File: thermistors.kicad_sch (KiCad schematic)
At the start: 6 parts, among them J6 Conn_02x10_Counter_Clockwise, J7 Conn_02x10_Counter_Clockwise, J8 Conn_02x10_Counter_Clockwise

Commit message: schematic: MCU cleanup
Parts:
- J6, J7, J8: footprint (none) -> Connector_JST:JST_PUD_S20B-PUDSS-1_2x10_P2.00mm_Horizontal; Part Number (none) -> S20B-PUDSS-1
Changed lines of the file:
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@@
 			)
 		)
-		(property "Footprint" ""
+		(property "Footprint" "Connector_JST:JST_PUD_S20B-PUDSS-1_2x10_P2.00mm_Horizontal"
 			(at 139.7 69.85 0)
 			(effects
@@
 		)
 		(property "Description" "Generic connector, double row, 02x10, counter clockwise pin numbering scheme (similar to DIP package numbering), script generated (kicad-library-utils/schlib/autogen/connector/)"
+			(at 139.7 69.85 0)
+			(effects
+				(font
+					(size 1.27 1.27)
+				)
+				(hide yes)
+			)
+		)
+		(property "Part Number" "S20B-PUDSS-1"
 			(at 139.7 69.85 0)
 			(effects
@@
 			)
 		)
-		(property "Footprint" ""
+		(property "Footprint" "Connector_JST:JST_PUD_S20B-PUDSS-1_2x10_P2.00mm_Horizontal"
 			(at 139.7 95.25 0)
 			(effects
@@
 		)
 		(property "Description" "Generic connector, double row, 02x10, counter clockwise pin numbering scheme (similar to DIP package numbering), script generated (kicad-library-utils/schlib/autogen/connector/)"
+			(at 139.7 95.25 0)
+			(effects
+				(font
+					(size 1.27 1.27)
+				)
+				(hide yes)
+			)
+		)
+		(property "Part Number" "S20B-PUDSS-1"
 			(at 139.7 95.25 0)
 			(effects
@@
 			)
 		)
-		(property "Footprint" ""
+		(property "Footprint" "Connector_JST:JST_PUD_S20B-PUDSS-1_2x10_P2.00mm_Horizontal"
 			(at 139.7 120.65 0)
 			(effects
@@
 			(at 139.7 120.65 0)
 			(effects
+				(font
+					(size 1.27 1.27)
+				)
+				(hide yes)
+			)
+		)
+		(property "Part Number" "S20B-PUDSS-1"
+			(at 139.7 120.65 0)
+			(effects

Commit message: schematic: Cleanup
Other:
- company: (none) -> York Formula Student
- title: (none) -> Battery Management System
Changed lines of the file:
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@@
 	(generator_version "8.0")
 	(paper "A4")
+	(title_block
+		(title "Battery Management System")
+		(date "2025-02-08")
+		(rev "1")
+		(company "York Formula Student")
+	)
 	(wire
 		(pts

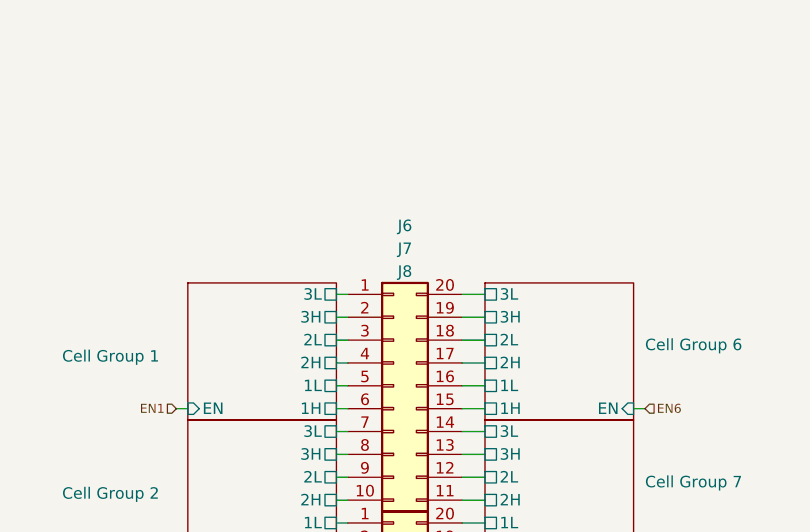
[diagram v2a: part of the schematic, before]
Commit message: schematic: Re-annotate designators
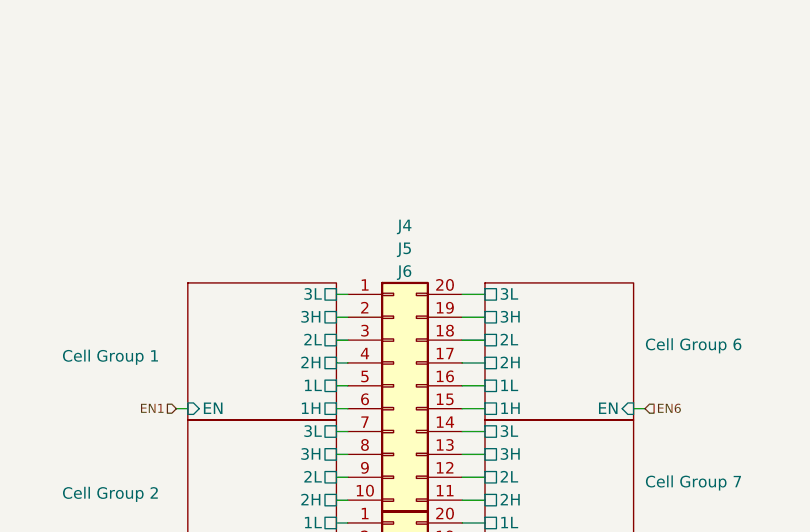
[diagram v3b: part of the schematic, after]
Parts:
- J4: renamed from J6; value Conn_02x10_Counter_Clockwise -> THERM_1; Role (none) -> Thermistor connector
- J5: renamed from J7; value Conn_02x10_Counter_Clockwise -> THERM_2; Role (none) -> Thermistor connector
- J6: renamed from J8; value Conn_02x10_Counter_Clockwise -> THERM_3; Role (none) -> Thermistor connector
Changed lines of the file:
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@@
 		(on_board yes)
 		(dnp no)
-		(property "Reference" "J6"
+		(property "Reference" "J4"
 			(at 140.97 52.07 0)
 			(effects
@@
 			)
 		)
-		(property "Value" "Conn_02x10_Counter_Clockwise"
+		(property "Value" "THERM_1"
 			(at 140.97 55.88 0)
 			(effects
@@
 		)
 		(property "Part Number" "S20B-PUDSS-1"
+			(at 139.7 69.85 0)
+			(effects
+				(font
+					(size 1.27 1.27)
+				)
+				(hide yes)
+			)
+		)
+		(property "Role" "Thermistor connector"
 			(at 139.7 69.85 0)
 			(effects
@@
 			(project "bms"
 				(path "/ae4a7653-8e6d-4e05-b144-1e5e3b2092b7/22f96080-372f-4edc-adbb-6967cdfa7222"
-					(reference "J6")
+					(reference "J4")
 					(unit 1)
 				)
@@
 		(on_board yes)
 		(dnp no)
-		(property "Reference" "J7"
+		(property "Reference" "J5"
 			(at 140.97 54.61 0)
 			(effects
@@
 			)
 		)
-		(property "Value" "Conn_02x10_Counter_Clockwise"
+		(property "Value" "THERM_2"
 			(at 140.97 81.28 0)
 			(effects
@@
 		)
 		(property "Part Number" "S20B-PUDSS-1"
+			(at 139.7 95.25 0)
+			(effects
+				(font
+					(size 1.27 1.27)
+				)
+				(hide yes)
+			)
+		)
+		(property "Role" "Thermistor connector"
 			(at 139.7 95.25 0)
 			(effects
@@
 			(project "bms"
 				(path "/ae4a7653-8e6d-4e05-b144-1e5e3b2092b7/22f96080-372f-4edc-adbb-6967cdfa7222"
-					(reference "J7")
+					(reference "J5")
 					(unit 1)
 				)
@@
 		(on_board yes)
 		(dnp no)
-		(property "Reference" "J8"
+		(property "Reference" "J6"
 			(at 140.97 57.15 0)
 			(effects
@@
 			)
 		)
-		(property "Value" "Conn_02x10_Counter_Clockwise"
+		(property "Value" "THERM_3"
 			(at 140.97 106.68 0)
 			(effects
@@
 		)
 		(property "Part Number" "S20B-PUDSS-1"
+			(at 139.7 120.65 0)
+			(effects
+				(font
+					(size 1.27 1.27)
+				)
+				(hide yes)
+			)
+		)
+		(property "Role" "Thermistor connector"
 			(at 139.7 120.65 0)
 			(effects
@@
 			(project ""
 				(path "/ae4a7653-8e6d-4e05-b144-1e5e3b2092b7/22f96080-372f-4edc-adbb-6967cdfa7222"
-					(reference "J8")
+					(reference "J6")
 					(unit 1)
 				)

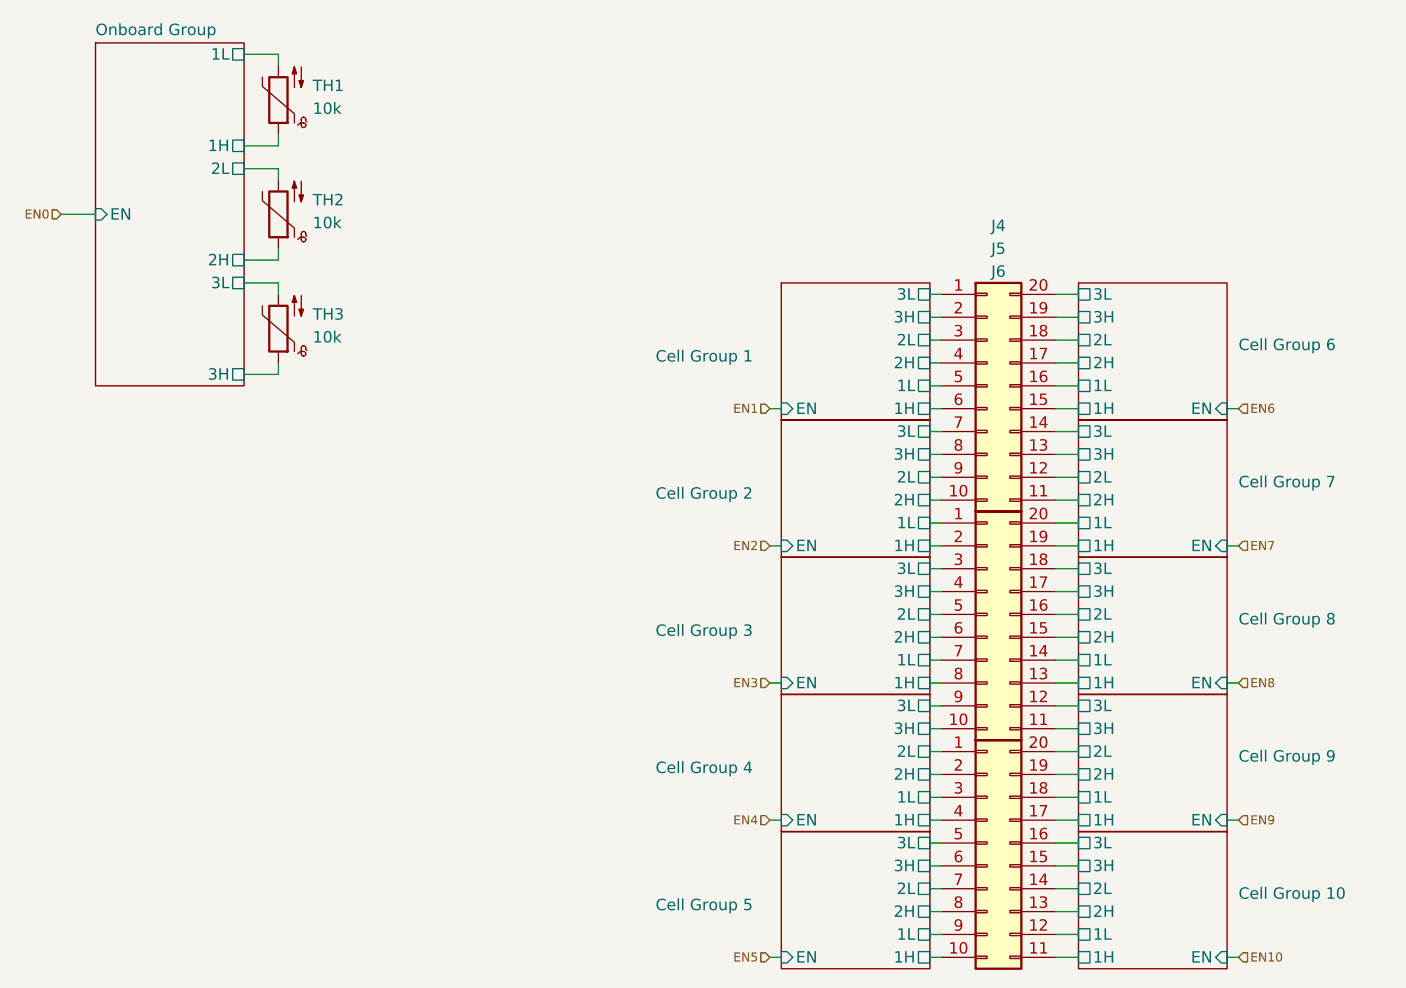
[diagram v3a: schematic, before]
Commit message: schematic: Don't make CV12 go through fuse and adjust thermistor pinout
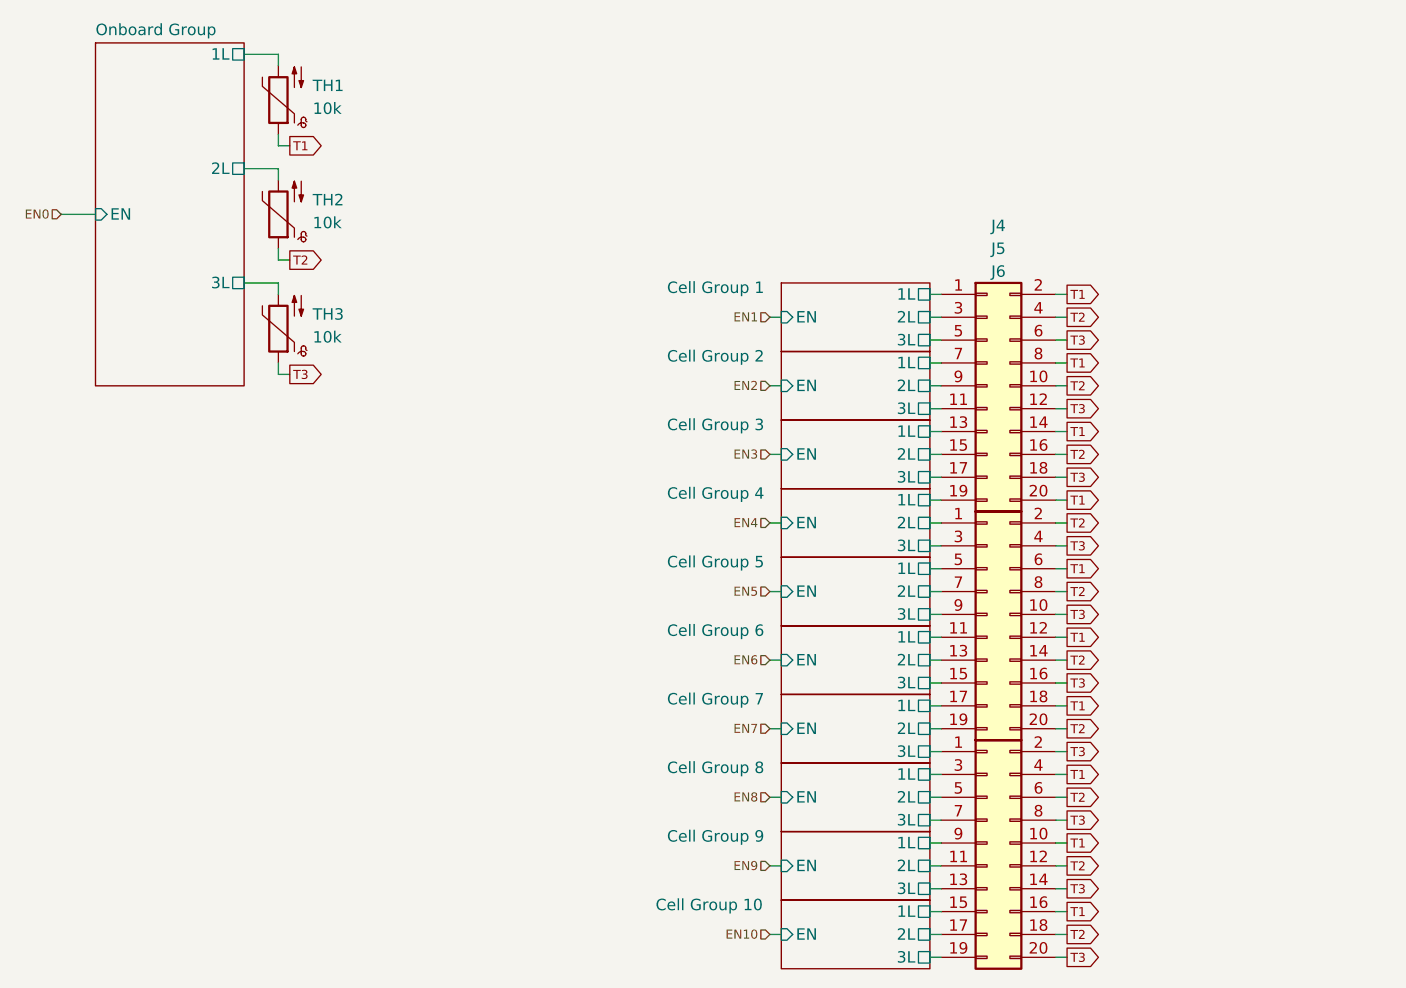
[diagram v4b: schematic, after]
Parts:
- J4, J5, J6: symbol Connector_Generic:Conn_02x10_Counter_Clockwise -> Connector_Generic:Conn_02x10_Odd_Even
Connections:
- net Cell Group 10/1H is gone; now on net Cell Group 9/2L: J6.11 (Pin_11)
- net Cell Group 10/2H is gone; now on net Cell Group 9/3L: J6.13 (Pin_13)
- net Cell Group 10/3H is gone; now on net Cell Group 10/1L: J6.15 (Pin_15)
- net Cell Group 2/1H is gone; now on net T2: J5.2 (Pin_2)
- net Cell Group 2/2H is gone; now on net T2: J4.10 (Pin_10)
- net Cell Group 2/3H is gone; now on net T1: J4.8 (Pin_8)
- net Cell Group 3/1H is gone; now on net T2: J5.8 (Pin_8)
- net Cell Group 3/2H is gone; now on net T1: J5.6 (Pin_6)
- net Cell Group 3/3H is gone; now on net T3: J5.4 (Pin_4)
- net Cell Group 4/1H is gone; now on net T1: J6.4 (Pin_4)
- net Cell Group 4/2H is gone; now on net T3: J6.2 (Pin_2)
- net Cell Group 4/3H is gone; now on net T3: J5.10 (Pin_10)
- net Cell Group 5/1H is gone; now on net T1: J6.10 (Pin_10)
- net Cell Group 5/2H is gone; now on net T3: J6.8 (Pin_8)
- net Cell Group 5/3H is gone; now on net T2: J6.6 (Pin_6)
- net Cell Group 6/1H is gone; now on net Cell Group 3/2L: J4.15 (Pin_15)
- net Cell Group 6/2H is gone; now on net Cell Group 3/3L: J4.17 (Pin_17)
- net Cell Group 6/3H is gone; now on net Cell Group 4/1L: J4.19 (Pin_19)
- net Cell Group 7/1H is gone; now on net Cell Group 7/2L: J5.19 (Pin_19)
- net Cell Group 7/2H is gone; now on net Cell Group 2/3L: J4.11 (Pin_11)
- net Cell Group 7/3H is gone; now on net Cell Group 3/1L: J4.13 (Pin_13)
- net Cell Group 8/1H is gone; now on net Cell Group 6/2L: J5.13 (Pin_13)
- net Cell Group 8/2H is gone; now on net Cell Group 6/3L: J5.15 (Pin_15)
- net Cell Group 8/3H is gone; now on net Cell Group 7/1L: J5.17 (Pin_17)
- net Cell Group 9/1H is gone; now on net Cell Group 10/2L: J6.17 (Pin_17)
- net Cell Group 9/2H is gone; now on net Cell Group 10/3L: J6.19 (Pin_19)
- net Cell Group 9/3H is gone; now on net Cell Group 6/1L: J5.11 (Pin_11)
- net Onboard Group/1H is gone; now on net T1: TH1.1
- net Onboard Group/2H is gone; now on net T2: TH2.1
- net Onboard Group/3H is gone; now on net T3: TH3.1
- net Cell Group 1/1L: now also J4.1 (Pin_1); no longer J4.5 (Pin_5)
- net Cell Group 1/3L: now also J4.5 (Pin_5); no longer J4.1 (Pin_1)
- net Cell Group 10/1L: no longer J6.12 (Pin_12)
- net Cell Group 10/2L: no longer J6.14 (Pin_14)
- net Cell Group 10/3L: no longer J6.16 (Pin_16)
- net Cell Group 2/1L: now also J4.7 (Pin_7); no longer J5.1 (Pin_1)
- net Cell Group 2/3L: no longer J4.7 (Pin_7)
- net Cell Group 3/1L: no longer J5.7 (Pin_7)
- net Cell Group 3/2L: no longer J5.5 (Pin_5)
- net Cell Group 3/3L: no longer J5.3 (Pin_3)
- net Cell Group 4/1L: no longer J6.3 (Pin_3)
- net Cell Group 4/2L: now also J5.1 (Pin_1); no longer J6.1 (Pin_1)
- net Cell Group 4/3L: now also J5.3 (Pin_3); no longer J5.9 (Pin_9)
- net Cell Group 5/1L: now also J5.5 (Pin_5); no longer J6.9 (Pin_9)
- net Cell Group 5/2L: now also J5.7 (Pin_7); no longer J6.7 (Pin_7)
- net Cell Group 5/3L: now also J5.9 (Pin_9); no longer J6.5 (Pin_5)
- net Cell Group 6/1L: no longer J4.16 (Pin_16)
- net Cell Group 6/2L: no longer J4.18 (Pin_18)
- net Cell Group 6/3L: no longer J4.20 (Pin_20)
- net Cell Group 7/1L: no longer J5.20 (Pin_20)
- net Cell Group 7/2L: no longer J4.12 (Pin_12)
- net Cell Group 7/3L: now also J6.1 (Pin_1); no longer J4.14 (Pin_14)
- net Cell Group 8/1L: now also J6.3 (Pin_3); no longer J5.14 (Pin_14)
- net Cell Group 8/2L: now also J6.5 (Pin_5); no longer J5.16 (Pin_16)
- net Cell Group 8/3L: now also J6.7 (Pin_7); no longer J5.18 (Pin_18)
- net Cell Group 9/1L: now also J6.9 (Pin_9); no longer J6.18 (Pin_18)
- net Cell Group 9/2L: no longer J6.20 (Pin_20)
- net Cell Group 9/3L: no longer J5.12 (Pin_12)
- net Cell Group 1/1H renamed T3
- net T3: now also J4.12 (Pin_12), J4.18 (Pin_18), J5.16 (Pin_16), J6.14 (Pin_14), J6.20 (Pin_20)
- net Cell Group 1/2H renamed T2
- net T2: now also J4.16 (Pin_16), J5.14 (Pin_14), J5.20 (Pin_20), J6.12 (Pin_12), J6.18 (Pin_18)
- net Cell Group 1/3H renamed T1
- net T1: now also J4.14 (Pin_14), J4.20 (Pin_20), J5.12 (Pin_12), J5.18 (Pin_18), J6.16 (Pin_16)
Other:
- sheet Cell Group 1 ports: added none; removed 1H, 2H, 3H
- sheet Cell Group 10 ports: added none; removed 1H, 2H, 3H
- sheet Cell Group 2 ports: added none; removed 1H, 2H, 3H
- sheet Cell Group 3 ports: added none; removed 1H, 2H, 3H
- sheet Cell Group 4 ports: added none; removed 1H, 2H, 3H
- sheet Cell Group 5 ports: added none; removed 1H, 2H, 3H
- sheet Cell Group 6 ports: added none; removed 1H, 2H, 3H
- sheet Cell Group 7 ports: added none; removed 1H, 2H, 3H
- sheet Cell Group 8 ports: added none; removed 1H, 2H, 3H
- sheet Cell Group 9 ports: added none; removed 1H, 2H, 3H
- sheet Onboard Group ports: added none; removed 1H, 2H, 3H

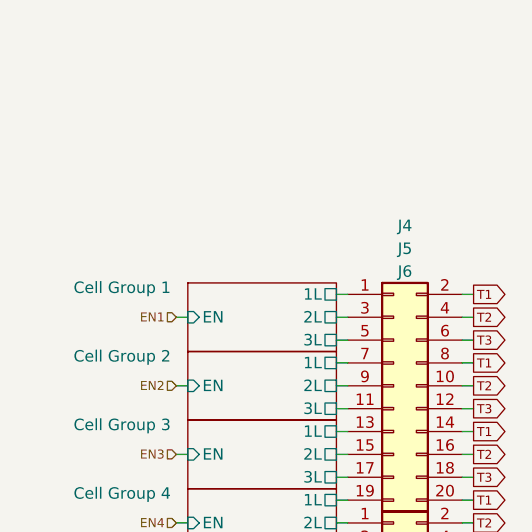
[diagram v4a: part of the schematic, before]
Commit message: schematic: Remove I2C_OUT connector
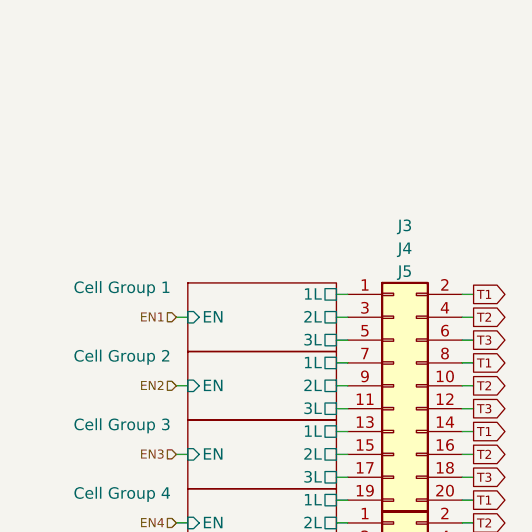
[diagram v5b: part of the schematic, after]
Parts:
- renumbered J4 to J3, J5 to J4, J6 to J5
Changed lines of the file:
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@@
 		(on_board yes)
 		(dnp no)
-		(property "Reference" "J4"
+		(property "Reference" "J3"
 			(at 140.97 52.07 0)
 			(effects
@@
 			(project "bms"
 				(path "/ae4a7653-8e6d-4e05-b144-1e5e3b2092b7/22f96080-372f-4edc-adbb-6967cdfa7222"
-					(reference "J4")
+					(reference "J3")
 					(unit 1)
 				)
@@
 		(on_board yes)
 		(dnp no)
-		(property "Reference" "J5"
+		(property "Reference" "J4"
 			(at 140.97 54.61 0)
 			(effects
@@
 			(project "bms"
 				(path "/ae4a7653-8e6d-4e05-b144-1e5e3b2092b7/22f96080-372f-4edc-adbb-6967cdfa7222"
-					(reference "J5")
+					(reference "J4")
 					(unit 1)
 				)
@@
 		(on_board yes)
 		(dnp no)
-		(property "Reference" "J6"
+		(property "Reference" "J5"
 			(at 140.97 57.15 0)
 			(effects
@@
 			(project ""
 				(path "/ae4a7653-8e6d-4e05-b144-1e5e3b2092b7/22f96080-372f-4edc-adbb-6967cdfa7222"
-					(reference "J6")
+					(reference "J5")
 					(unit 1)
 				)

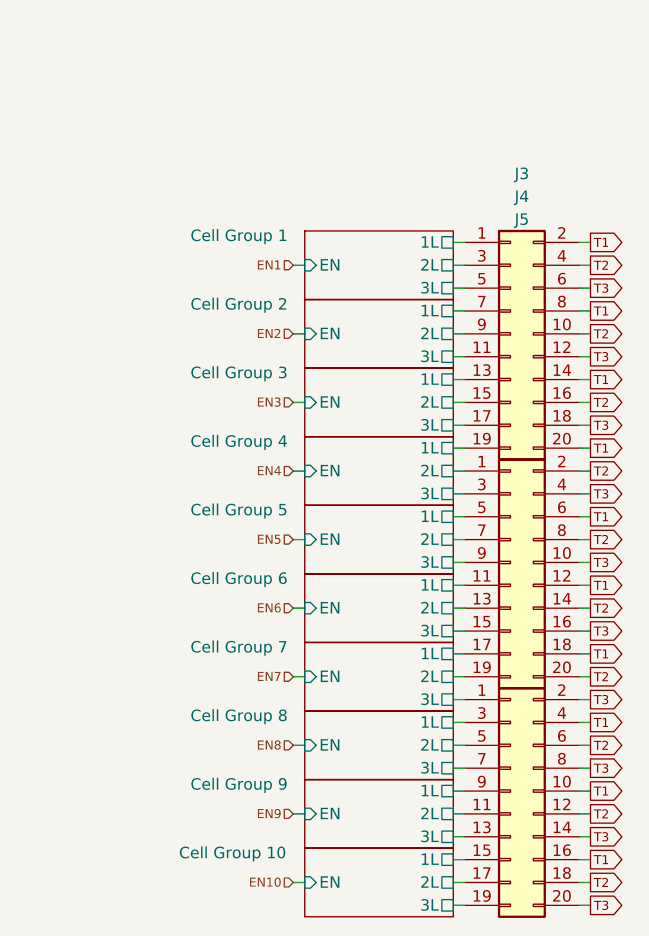
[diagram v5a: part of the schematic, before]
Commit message: schematic: Reduce down to two thermistor connectors
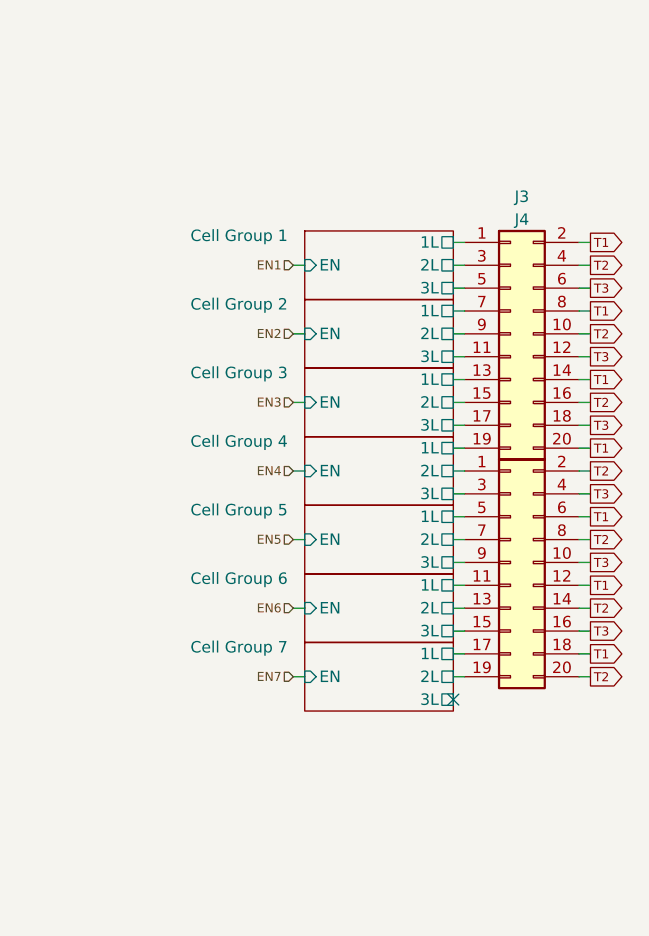
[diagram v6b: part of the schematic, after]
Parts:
- removed J5: THERM_3, Connector_JST:JST_PUD_S20B-PUDSS-1_2x10_P2.00mm_Horizontal, symbol Connector_Generic:Conn_02x10_Odd_Even
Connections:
- no-connect marks 0 -> 1
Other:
- removed sheet Cell Group 10
- removed sheet Cell Group 8
- removed sheet Cell Group 9
